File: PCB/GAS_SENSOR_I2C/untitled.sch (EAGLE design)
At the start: 40 parts, among them IC1 AZ1117CR2-5.0TRG1, IC2 LM393D, Q1 2N7002, Q2 2N7002, U2 LGT8F328P

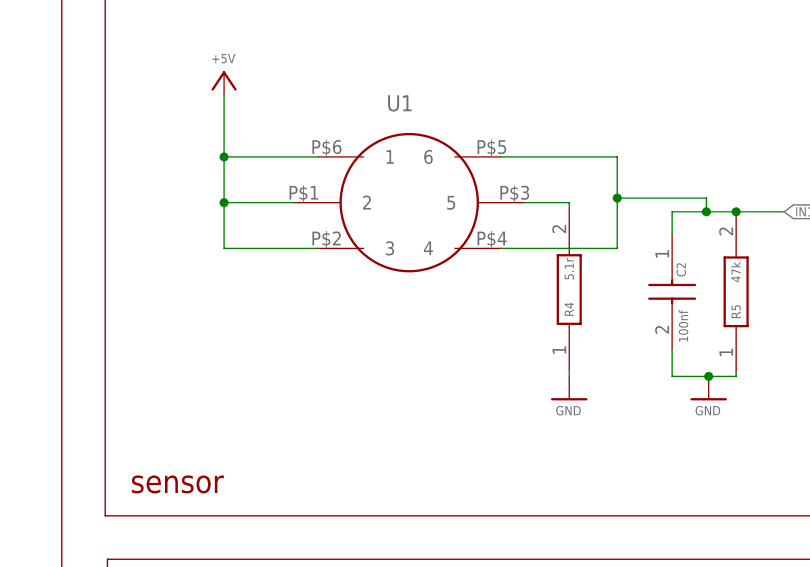
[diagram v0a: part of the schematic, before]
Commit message: FEAT: update mq socket footprint
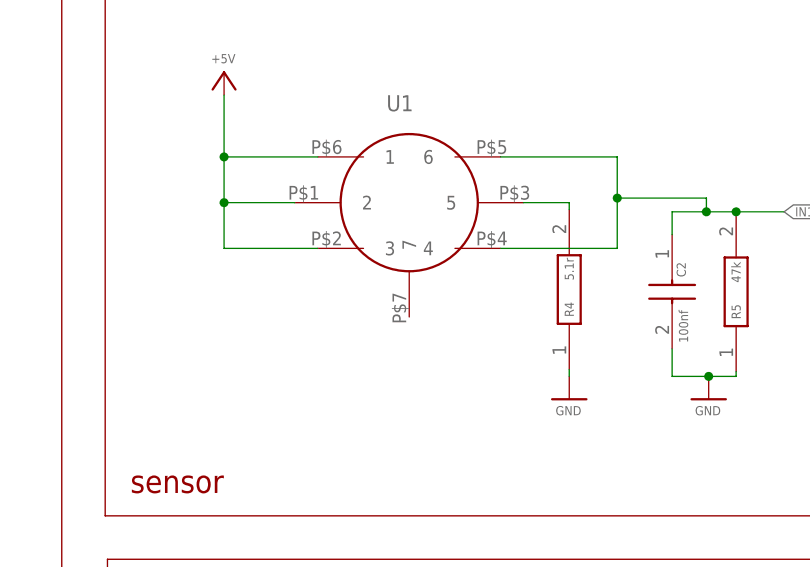
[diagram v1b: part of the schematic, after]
